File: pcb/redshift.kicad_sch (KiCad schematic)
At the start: 75 parts, among them J1 G-Switch GT-USB-7010ASV, J2 C145962, J3 C2935905, J4 Conn_ARM_JTAG_SWD_10, SW1 SW_SP, SW2 SW_SP, SW3 SW_SP, SW4 PTS810, U1 PAW3399DM‐T4QU, U2 MIC5365-3.3YC5-TR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

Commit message: Progress on the PCB routing
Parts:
- U4: footprint (none) -> LPC5528JBD64:QFP50P1200X1200X120-65N
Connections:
- net ENC_A: now also U4.45 (PIO0_24); no longer U4.39 (PIO1_1/WAKEUP)
- net ENC_B: now also U4.46 (PIO0_13); no longer U4.42 (PIO1_3)
- net FAULT_LED: now also U4.40 (PIO0_26); no longer U4.48 (PIO0_20)
- net SW1_L_NC: now also U4.48 (PIO0_20); no longer U4.17 (PIO0_8)
- net SW1_L_NO: now also U4.47 (PIO0_14); no longer U4.37 (PIO0_9/ACMP0_B)
- net SW4_NC: now also U4.3 (PIO0_17); no longer U4.51 (PIO0_25)
- net SW4_NO: now also U4.4 (PIO1_0/ADC0_11); no longer U4.49 (PIO0_21)
- net SW5_NC: now also U4.2 (PIO0_1); no longer U4.47 (PIO0_14)
- net SW5_NO: now also U4.1 (PIO0_7); no longer U4.46 (PIO0_13)
- net USB1_LED: now also U4.41 (PIO1_2); no longer U4.2 (PIO0_1)
- net USER_LED: now also U4.42 (PIO1_3); no longer U4.52 (PIO0_2/TRST)
- no-connect marks 4 -> 18

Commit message: Routing basically done
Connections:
- net SW2_R_NC: now also U4.35 (XTAL32K_N); no longer U4.38 (PIO0_18/ACMP0_C)
- net SW2_R_NO: now also U4.36 (PIO0_0/_ACMP0_A); no longer U4.53 (PIO0_3/TCK)
- net SW3_M_NC: now also U4.38 (PIO0_18/ACMP0_C); no longer U4.35 (XTAL32K_N)
- net SW3_M_NO: now also U4.39 (PIO1_1/WAKEUP); no longer U4.36 (PIO0_0/_ACMP0_A)

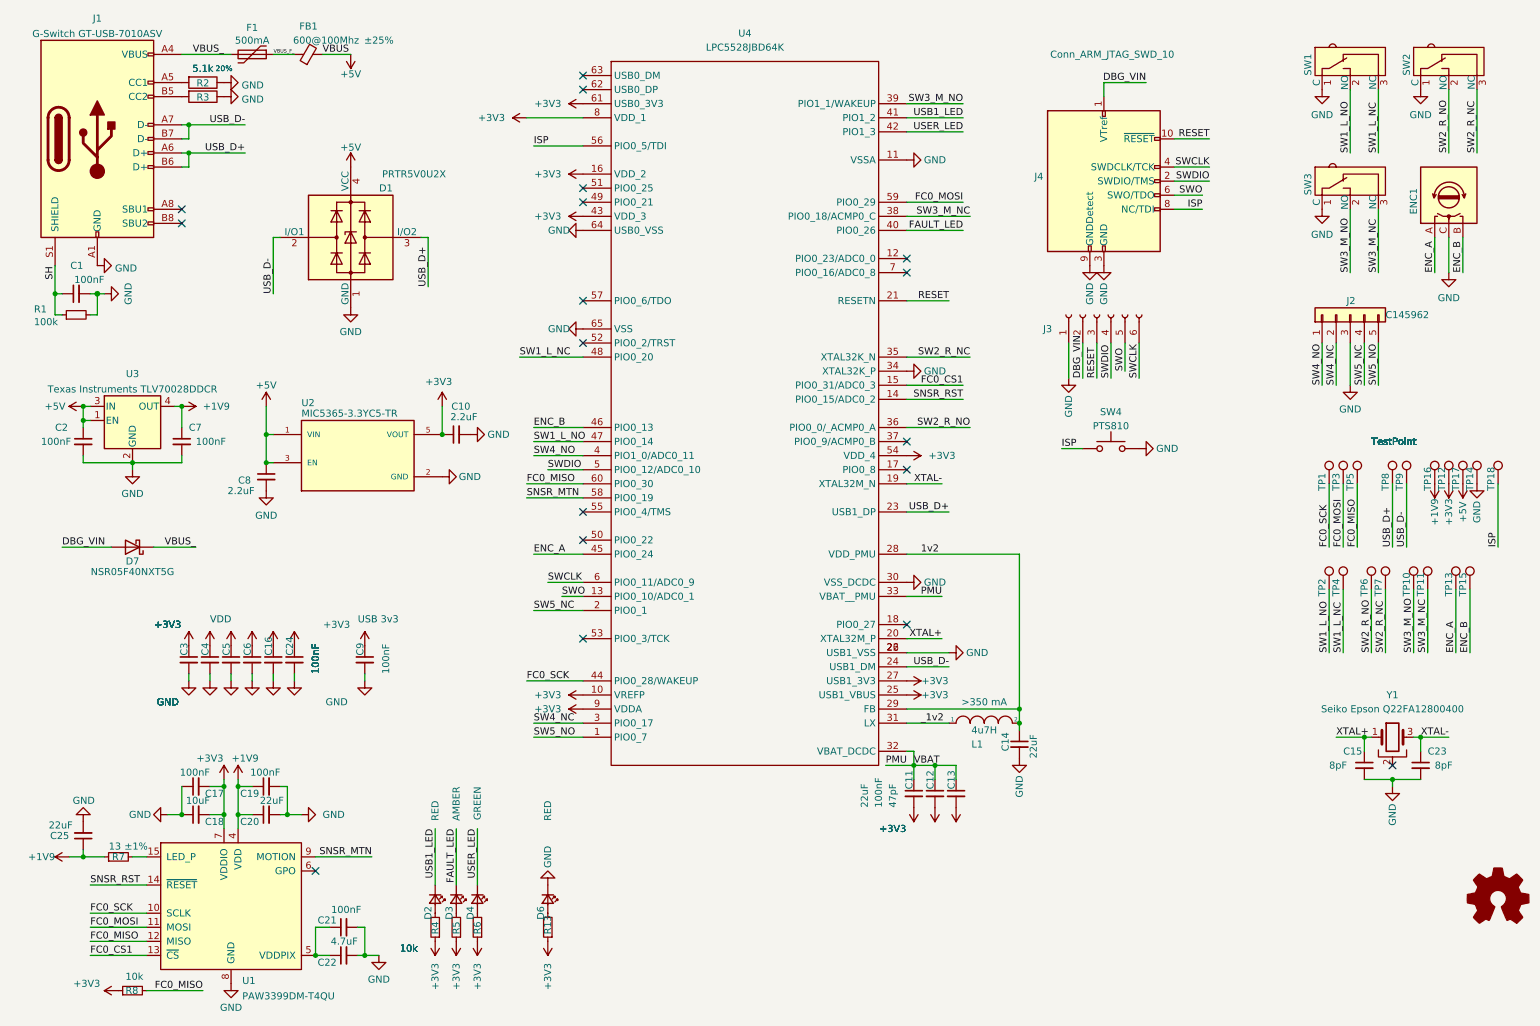
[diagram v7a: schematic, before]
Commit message: refactor mcu layout for better clarity
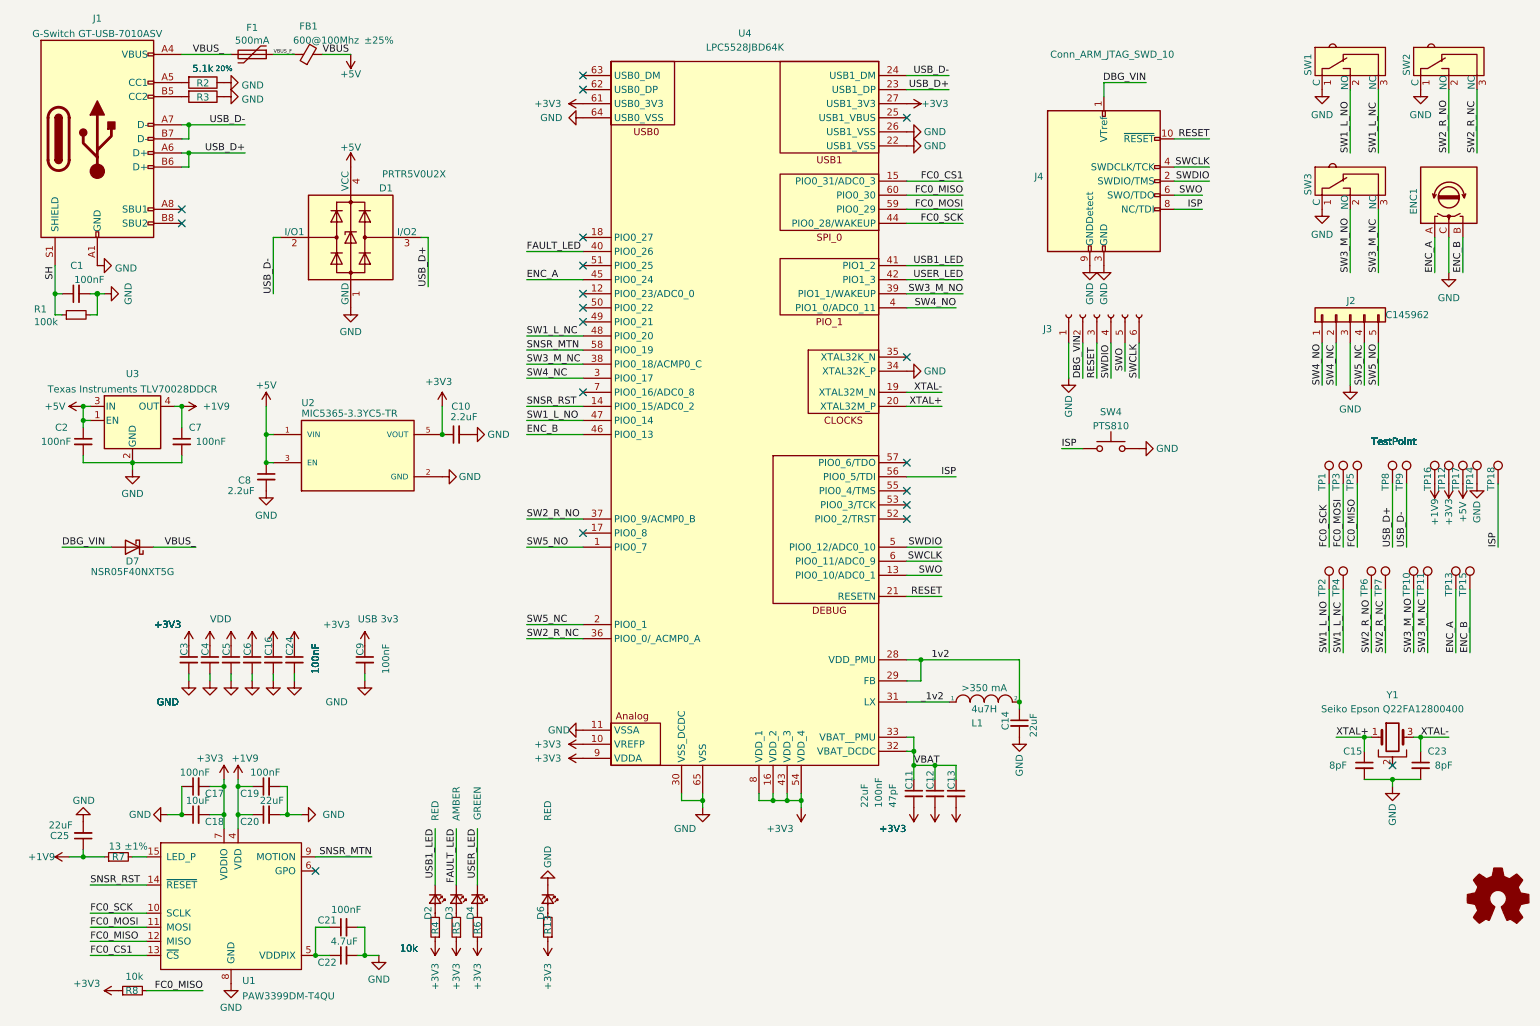
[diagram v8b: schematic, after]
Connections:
- net +3V3: no longer U4.25 (USB1_VBUS)
- net SW2_R_NC: now also U4.36 (PIO0_0/_ACMP0_A); no longer U4.35 (XTAL32K_N)
- net SW2_R_NO: now also U4.37 (PIO0_9/ACMP0_B); no longer U4.36 (PIO0_0/_ACMP0_A)
- net PMU renamed VBAT
- no-connect marks 18 -> 19
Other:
- moved on the sheet: C14, L1
